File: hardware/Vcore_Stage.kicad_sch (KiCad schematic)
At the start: 0 parts

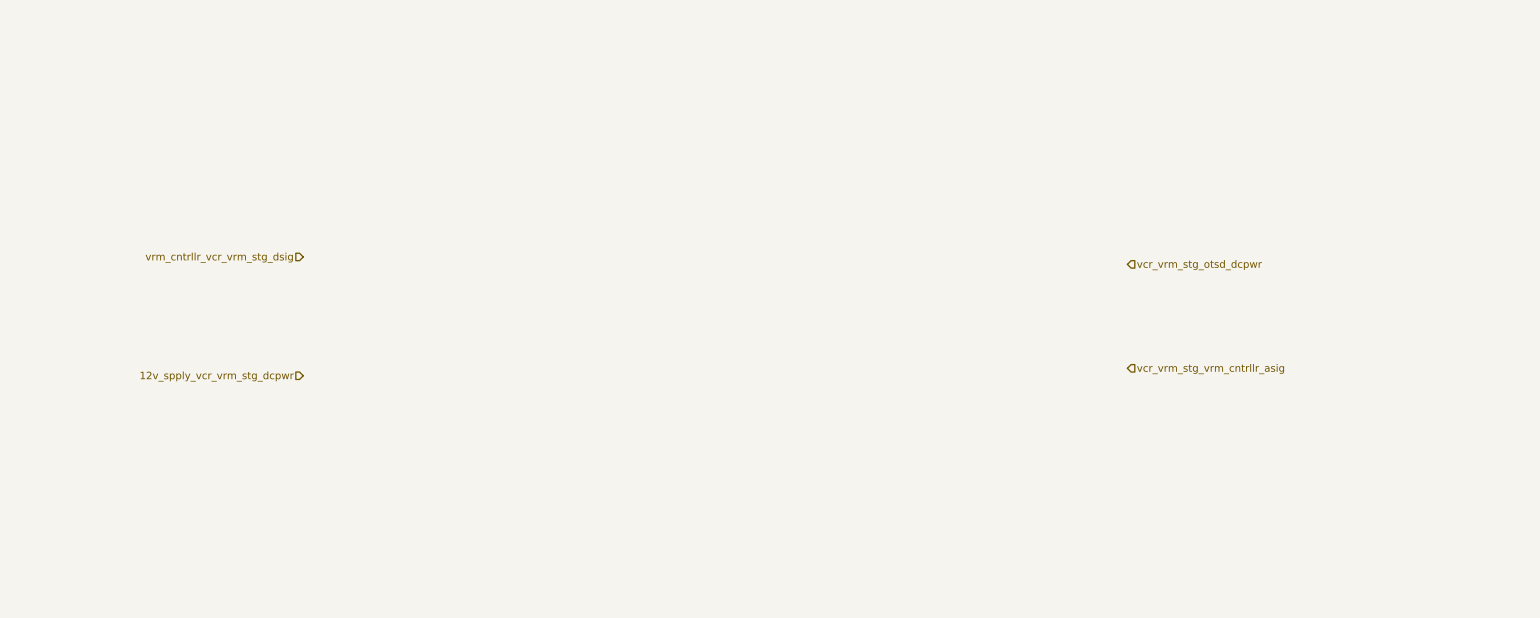
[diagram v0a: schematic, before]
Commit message: feat: Laid-out MOSFET ICs
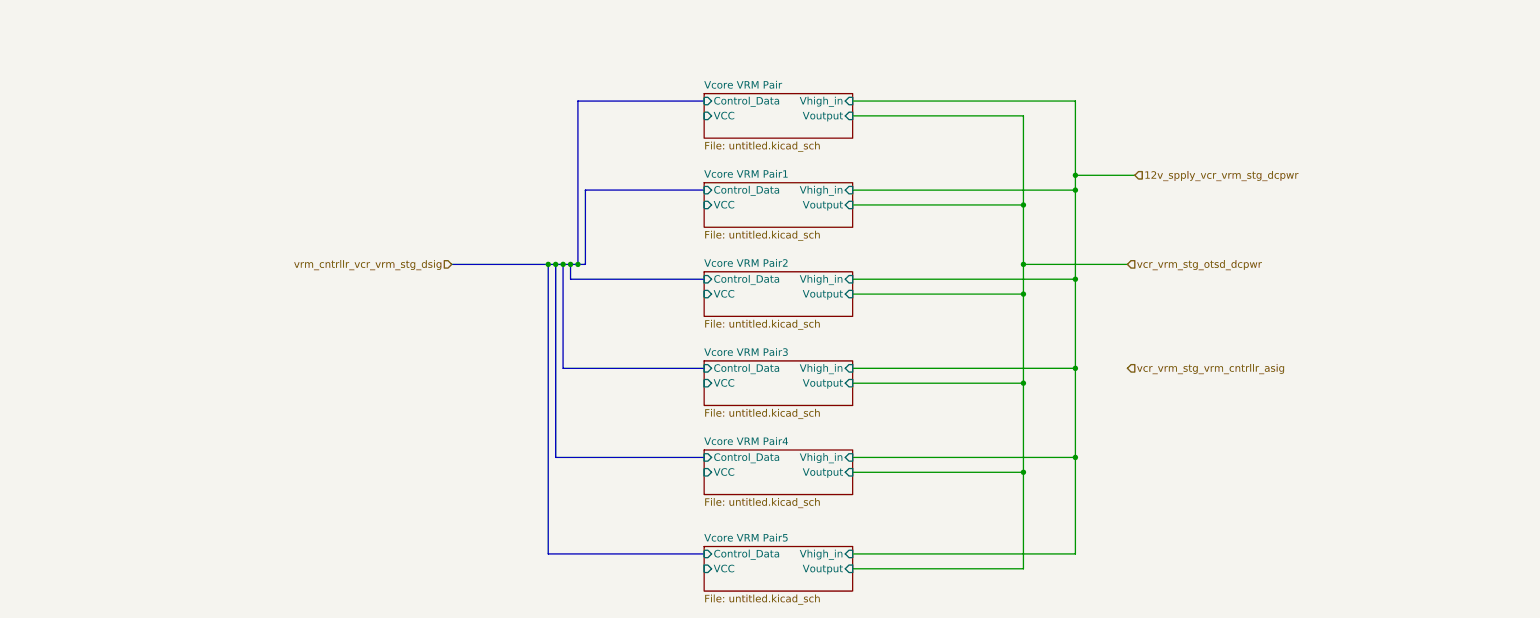
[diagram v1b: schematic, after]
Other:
- added sheet Vcore VRM Pair (untitled.kicad_sch)
- added sheet Vcore VRM Pair1 (untitled.kicad_sch)
- added sheet Vcore VRM Pair2 (untitled.kicad_sch)
- added sheet Vcore VRM Pair3 (untitled.kicad_sch)
- added sheet Vcore VRM Pair4 (untitled.kicad_sch)
- added sheet Vcore VRM Pair5 (untitled.kicad_sch)
- title: (none) -> Vcore VRM Stage

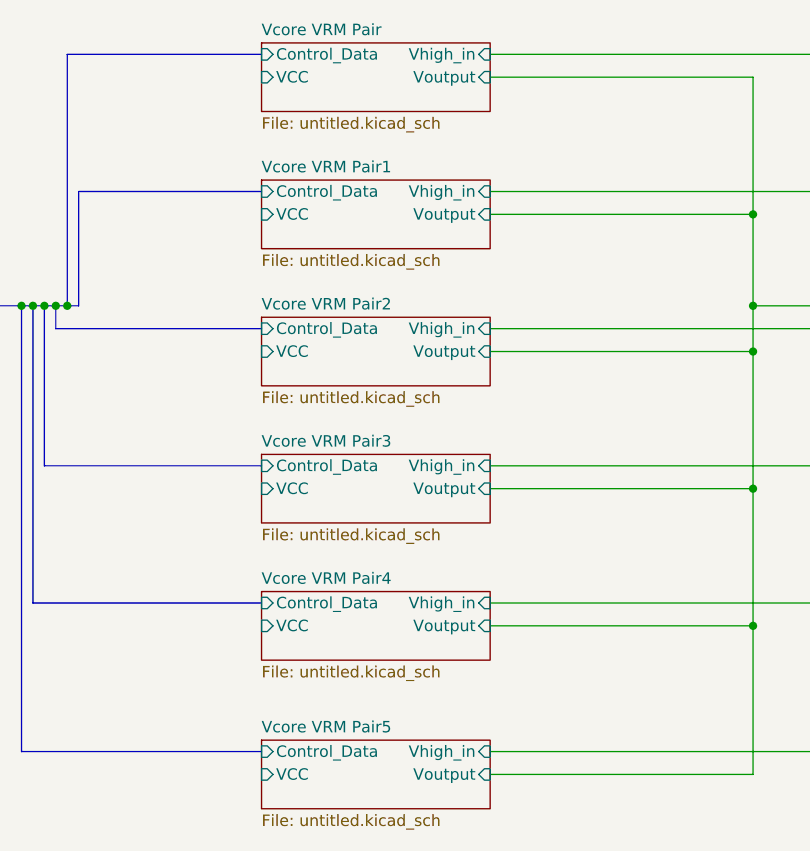
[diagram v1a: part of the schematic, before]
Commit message: chore: redirect sub-schematic from untitled to Double_Mos
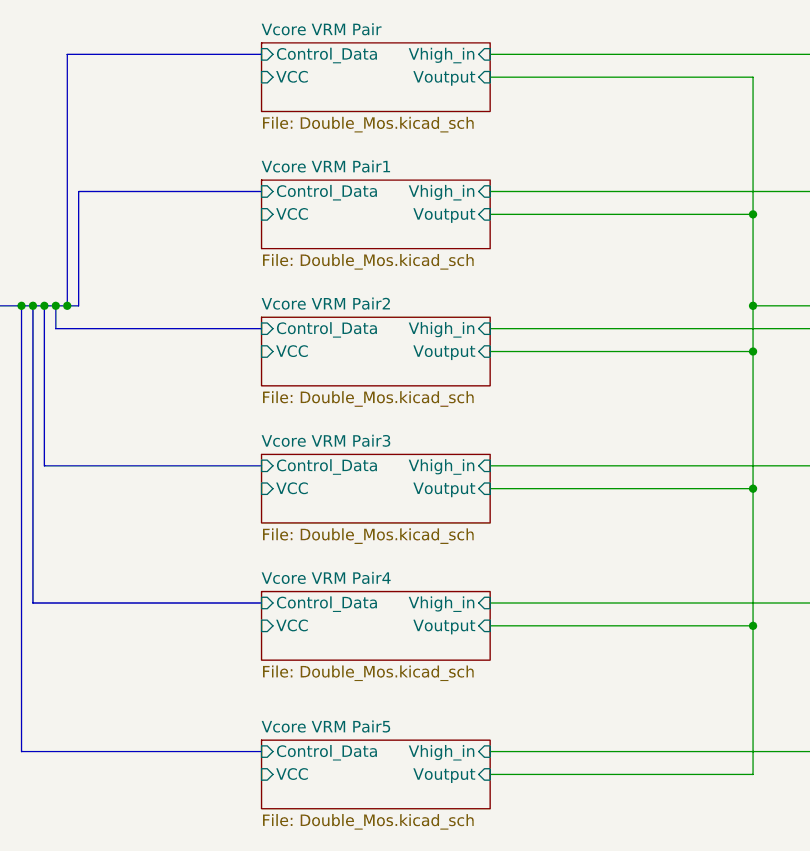
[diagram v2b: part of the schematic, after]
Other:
- sheet Vcore VRM Pair: file untitled.kicad_sch -> Double_Mos.kicad_sch
- sheet Vcore VRM Pair1: file untitled.kicad_sch -> Double_Mos.kicad_sch
- sheet Vcore VRM Pair2: file untitled.kicad_sch -> Double_Mos.kicad_sch
- sheet Vcore VRM Pair3: file untitled.kicad_sch -> Double_Mos.kicad_sch
- sheet Vcore VRM Pair4: file untitled.kicad_sch -> Double_Mos.kicad_sch
- sheet Vcore VRM Pair5: file untitled.kicad_sch -> Double_Mos.kicad_sch
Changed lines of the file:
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@@
 			)
 		)
-		(property "Sheetfile" "untitled.kicad_sch"
+		(property "Sheetfile" "Double_Mos.kicad_sch"
 			(at 133.35 100.9146 0)
 			(effects
@@
 			)
 		)
-		(property "Sheetfile" "untitled.kicad_sch"
+		(property "Sheetfile" "Double_Mos.kicad_sch"
 			(at 133.35 117.4246 0)
 			(effects
@@
 			)
 		)
-		(property "Sheetfile" "untitled.kicad_sch"
+		(property "Sheetfile" "Double_Mos.kicad_sch"
 			(at 133.35 55.1946 0)
 			(effects
@@
 			)
 		)
-		(property "Sheetfile" "untitled.kicad_sch"
+		(property "Sheetfile" "Double_Mos.kicad_sch"
 			(at 133.35 39.9546 0)
 			(effects
@@
 			)
 		)
-		(property "Sheetfile" "untitled.kicad_sch"
+		(property "Sheetfile" "Double_Mos.kicad_sch"
 			(at 133.35 85.6746 0)
 			(effects
@@
 			)
 		)
-		(property "Sheetfile" "untitled.kicad_sch"
+		(property "Sheetfile" "Double_Mos.kicad_sch"
 			(at 133.35 70.4346 0)
 			(effects

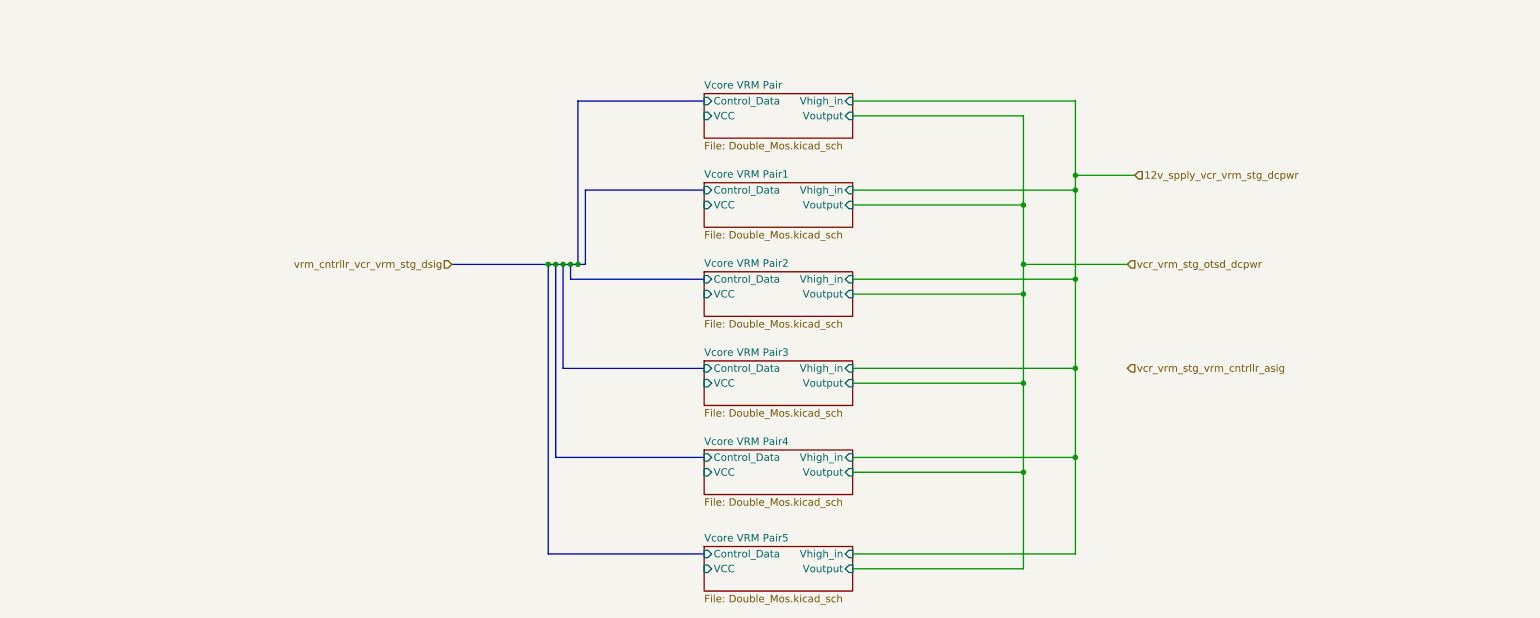
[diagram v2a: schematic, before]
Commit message: rebase(schematic): Updated Vcore and Vmem pins
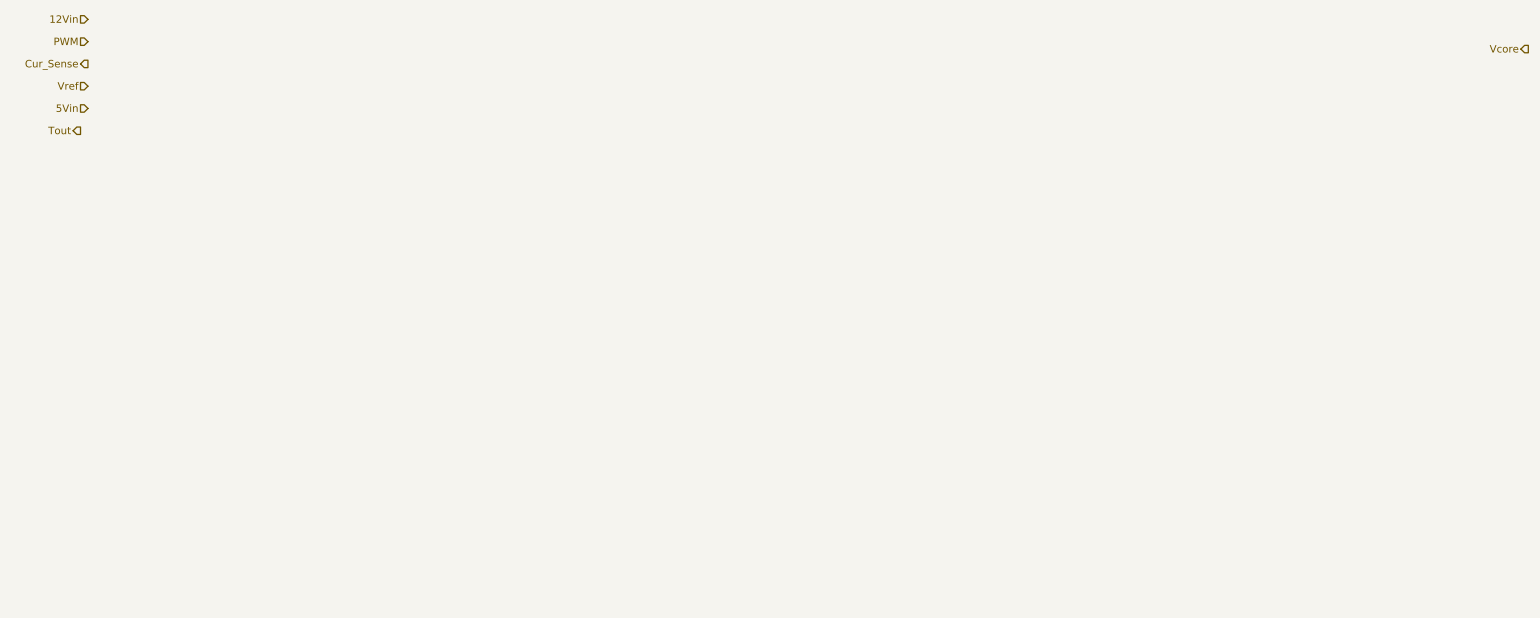
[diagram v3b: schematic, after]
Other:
- removed sheet Vcore VRM Pair
- removed sheet Vcore VRM Pair1
- removed sheet Vcore VRM Pair2
- removed sheet Vcore VRM Pair3
- removed sheet Vcore VRM Pair4
- removed sheet Vcore VRM Pair5

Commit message: feet(schematic): Vcore schematic made
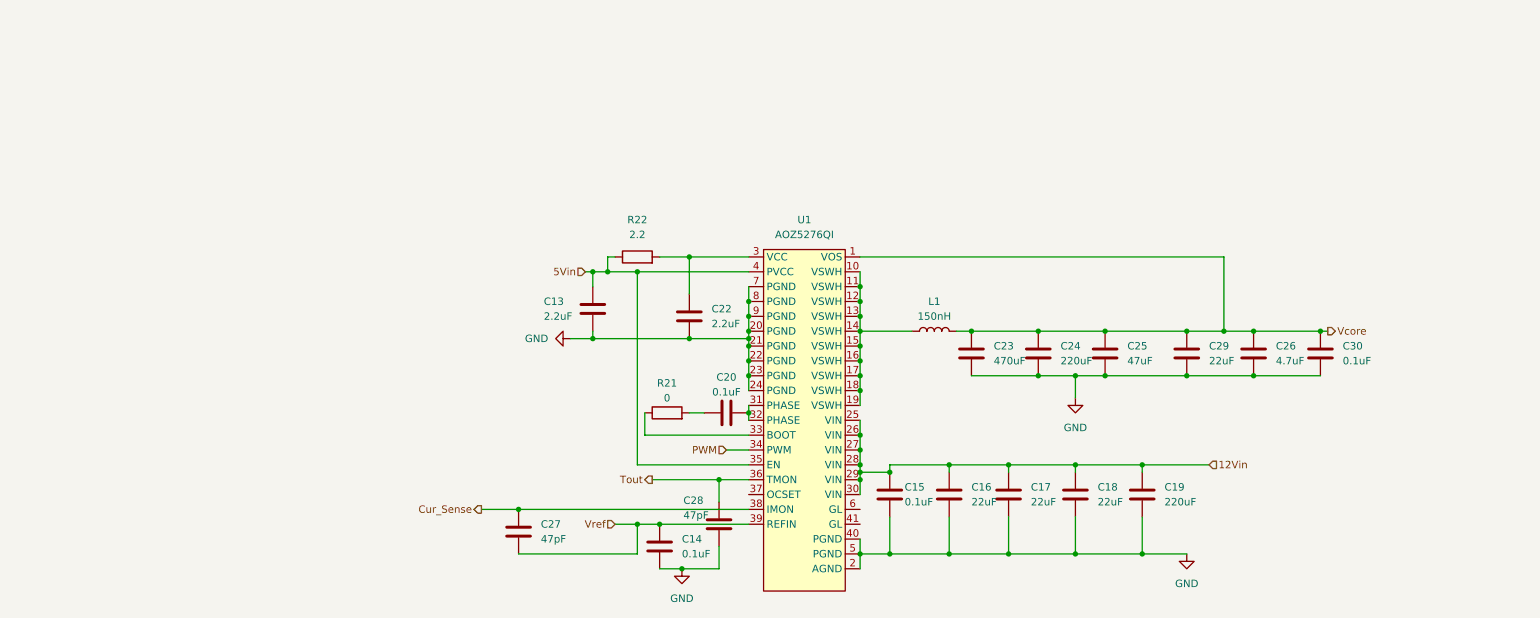
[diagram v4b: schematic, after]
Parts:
- added C13, C22: 2.2uF, symbol Device:C
- added C14, C15, C20, C30: 0.1uF, symbol Device:C
- added C16, C17, C18, C29: 22uF, symbol Device:C
- added C19, C24: 220uF, symbol Device:C
- added C23: 470uF, symbol Device:C
- added C25: 47uF, symbol Device:C
- added C26: 4.7uF, symbol Device:C
- added C27, C28: 47pF, symbol Device:C
- added L1: 150nH, symbol Device:L
- added R21: 0, symbol Device:R
- added R22: 2.2, symbol Device:R
- added U1: AOZ5276QI, symbol Symbol_Library:AOZ5276QI
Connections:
- net 12Vin: now also C15.1, C16.1, C17.1, C18.1, C19.1, U1.25 (VIN), U1.26 (VIN), U1.27 (VIN), U1.28 (VIN), U1.29 (VIN), U1.30 (VIN)
- net 5Vin: now also C13.1, R22.1, U1.35 (EN), U1.4 (PVCC)
- net Cur_Sense: now also C27.1, U1.38 (IMON)
- net PWM: now also U1.34 (PWM)
- net Tout: now also C28.1, U1.36 (TMON)
- net Vcore: now also C23.1, C24.1, C25.1, C26.1, C29.1, C30.1, L1.2, U1.1 (VOS)
- net Vref: now also C14.1, C27.2, U1.39 (REFIN)
- new net: C22.1, R22.2, U1.3 (VCC)
- new net: R21.1, U1.33 (BOOT)
- new net: C20.1, R21.2
- new net: C20.2, U1.31 (PHASE), U1.32 (PHASE)
- new net: L1.1, U1.10 (VSWH), U1.11 (VSWH), U1.12 (VSWH), U1.13 (VSWH), U1.14 (VSWH), U1.15 (VSWH), U1.16 (VSWH), U1.17 (VSWH), U1.18 (VSWH), U1.19 (VSWH)
- new net GND: C13.2, C14.2, C15.2, C16.2, C17.2, C18.2, C19.2, C22.2, C23.2, C24.2, C25.2, C26.2, C28.2, C29.2, C30.2, U1.2 (AGND), U1.20 (PGND), U1.21 (PGND), U1.22 (PGND), U1.23 (PGND), U1.24 (PGND), U1.40 (PGND), U1.5 (PGND), U1.7 (PGND), U1.8 (PGND), U1.9 (PGND)

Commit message: feat(schematic): Vmem schematic completed, connected controler and stages on main
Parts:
- C11001: renamed from C27; footprint (none) -> Capacitor_SMD:C_0805_2012Metric
- C11002: renamed from C13; footprint (none) -> Capacitor_SMD:C_0805_2012Metric
- C11003: renamed from C14; footprint (none) -> Capacitor_SMD:C_0805_2012Metric
- C11004: renamed from C22; footprint (none) -> Capacitor_SMD:C_0805_2012Metric
- C11005: renamed from C28; footprint (none) -> Capacitor_SMD:C_0805_2012Metric
- C11006: renamed from C20; footprint (none) -> Capacitor_SMD:C_0805_2012Metric
- C11007: renamed from C15; footprint (none) -> Capacitor_SMD:C_0805_2012Metric
- C11008: renamed from C16; footprint (none) -> Capacitor_SMD:C_0805_2012Metric
- C11009: renamed from C23; footprint (none) -> work:CP_EIA-7343-40_Kemet-Y
- C11010: renamed from C17; footprint (none) -> Capacitor_SMD:C_0805_2012Metric
- C11011: renamed from C24; footprint (none) -> Capacitor_THT:CP_Radial_D6.3mm_P2.50mm
- C11012: renamed from C18; footprint (none) -> Capacitor_SMD:C_0805_2012Metric
- C11013: renamed from C25; footprint (none) -> Capacitor_SMD:C_0805_2012Metric
- C11014: renamed from C19; footprint (none) -> Capacitor_THT:CP_Radial_D6.3mm_P2.50mm
- C11015: renamed from C29; footprint (none) -> Capacitor_SMD:C_0805_2012Metric
- C11016: renamed from C26; footprint (none) -> Capacitor_SMD:C_0805_2012Metric
- C11017: renamed from C30; footprint (none) -> Capacitor_SMD:C_0805_2012Metric
- L11001: renamed from L1; footprint (none) -> work:IND_IHVR-4025JZ-3Z_VIS
- R11001: renamed from R22; footprint (none) -> Resistor_SMD:R_0805_2012Metric
- R11002: renamed from R21; footprint (none) -> Resistor_SMD:R_0805_2012Metric
- U11001: renamed from U1; footprint (none) -> work:AOZ5276QI
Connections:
- net Tout renamed CORE_TEMP

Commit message: feat(schematic): add feedback pins
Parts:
- renumbered C11001 to C16018, C11002 to C16019, C11003 to C16020, C11004 to C16021, C11005 to C16022, C11006 to C16023, C11007 to C16024, C11008 to C16025, C11009 to C16026, C11010 to C16027, C11011 to C16028, C11012 to C16029, C11013 to C16030, C11014 to C16031, C11015 to C16032, C11016 to C16033, C11017 to C16034, L11001 to L16002, R11001 to R16003, R11002 to R16004, U11001 to U16002

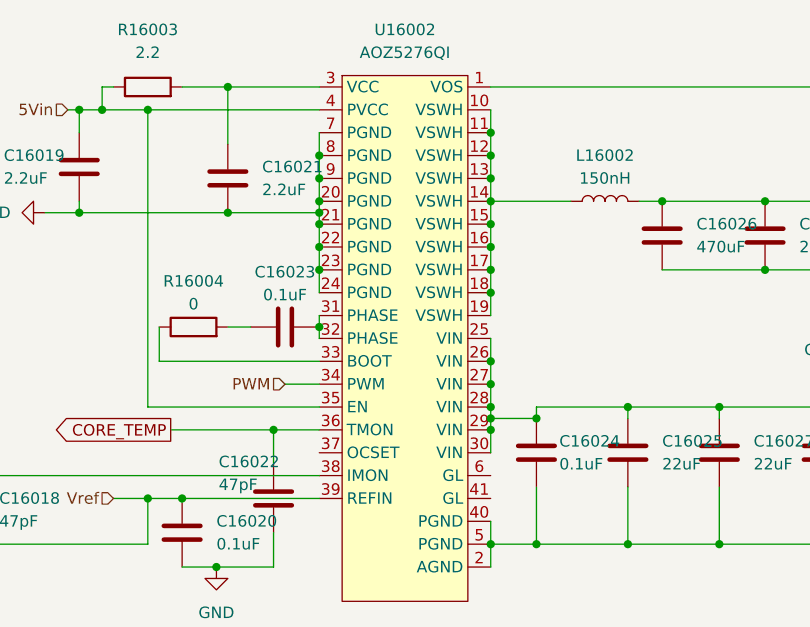
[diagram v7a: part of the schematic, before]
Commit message: feat(PCB): fix all DRC errors
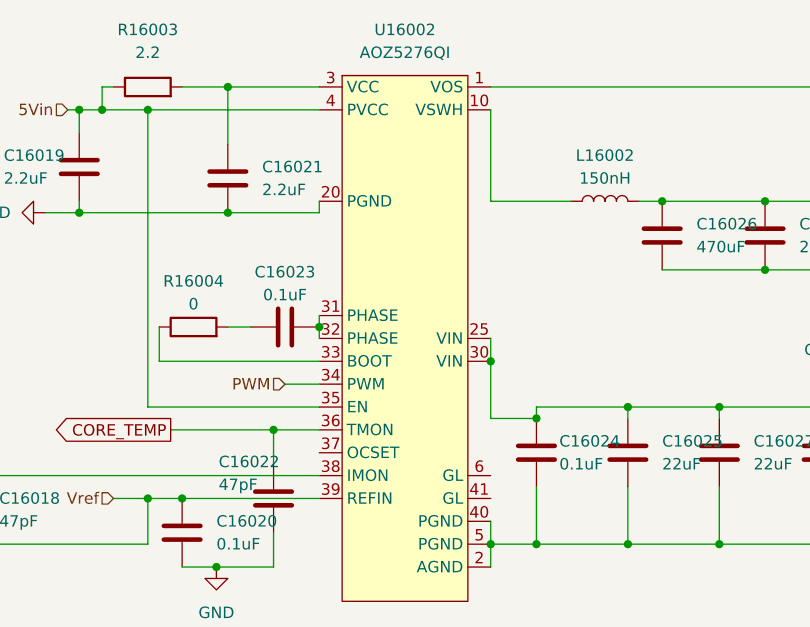
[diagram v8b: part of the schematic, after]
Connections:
- net 12Vin: no longer U16002.26 (VIN), U16002.27 (VIN), U16002.28 (VIN), U16002.29 (VIN)
- net GND: no longer U16002.21 (PGND), U16002.22 (PGND), U16002.23 (PGND), U16002.24 (PGND), U16002.7 (PGND), U16002.8 (PGND), U16002.9 (PGND)
- new net: L16002.1, U16002.10 (VSWH)
